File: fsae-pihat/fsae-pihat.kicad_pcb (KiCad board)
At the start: 4 copper layers, 85 x 56 mm, 67 parts, among them J1 Conn_02x02_Odd_Even, J2 Raspberry_Pi_4, J3 Conn_01x03_Pin, J4 1-2834011-4, J5 1-2834011-4, U1 TPS5430DDAR, U2 PCF8563T, U3 MCP2515-xST, U4 SN65HVD230DR-JSM, U5 TPS1H200AQDGNRQ1, X1 Q13FC1350000400, X2 X322512MSB4SI

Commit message: feat: readme, journal, pcb updates
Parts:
- added JP2: Jumper_3_Open, Connector_PinHeader_2.54mm:PinHeader_1x03_P2.54mm_Vertical, F.Cu at (187.3, 81.7)
- D11, D12, D2, D3: value SS34 -> SS54; footprint Diode_SMD:D_SMA -> PCM_JLCPCB:D_SMA
- moved D1 2.61 mm to (191.1, 83.8)
- moved D4 1.85 mm to (196.4, 92.2)
- moved J1 1.81 mm to (197.7, 86.0)
- moved F1 1.67 mm to (195.8, 81.8)
- moved J3 0.80 mm to (176.6, 103.5)
- moved D11 0.10 mm to (130.8, 116.8)
- moved D12 0.10 mm to (130.8, 113.0)
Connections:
- D1 pad 2: +24V-CAR -> /24V-RAW
- F1 pad 1: +24V-CAR -> /24V-RAW
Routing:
- net /CANL: track 23.8 -> 26.1 mm
- net /CANH: track 20.4 -> 22.4 mm
- net Net-(ETH1-A_YELLOW): track 20.5 -> 22.4 mm
- net GND: track 27.8 -> 27.1 mm
- net +24V-CAR: vias 52 -> 30
- added copper zone on F.Cu, net /24V-RAW
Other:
- board text added: "1.5A MAX"
- board text added: "EN"
- board text removed: "2A MAX"

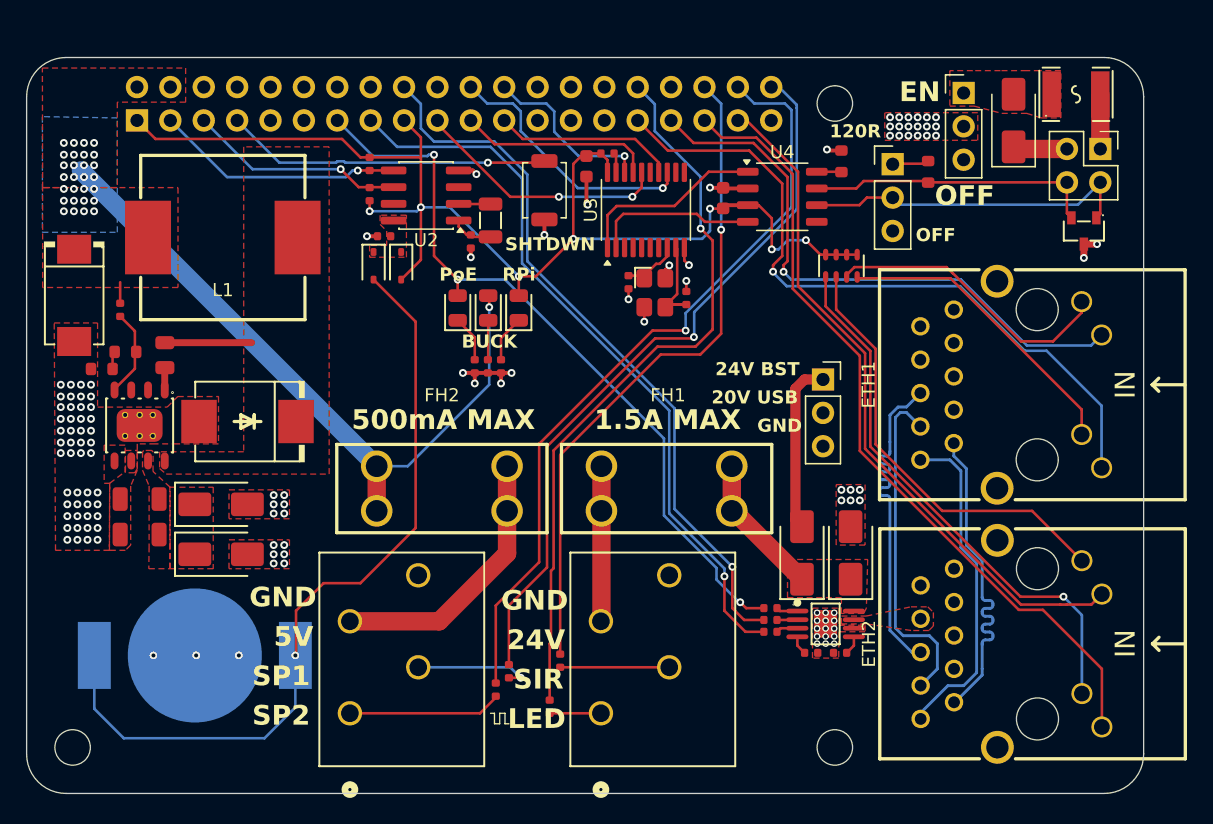
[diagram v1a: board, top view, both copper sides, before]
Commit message: feat: pcb art and updated design
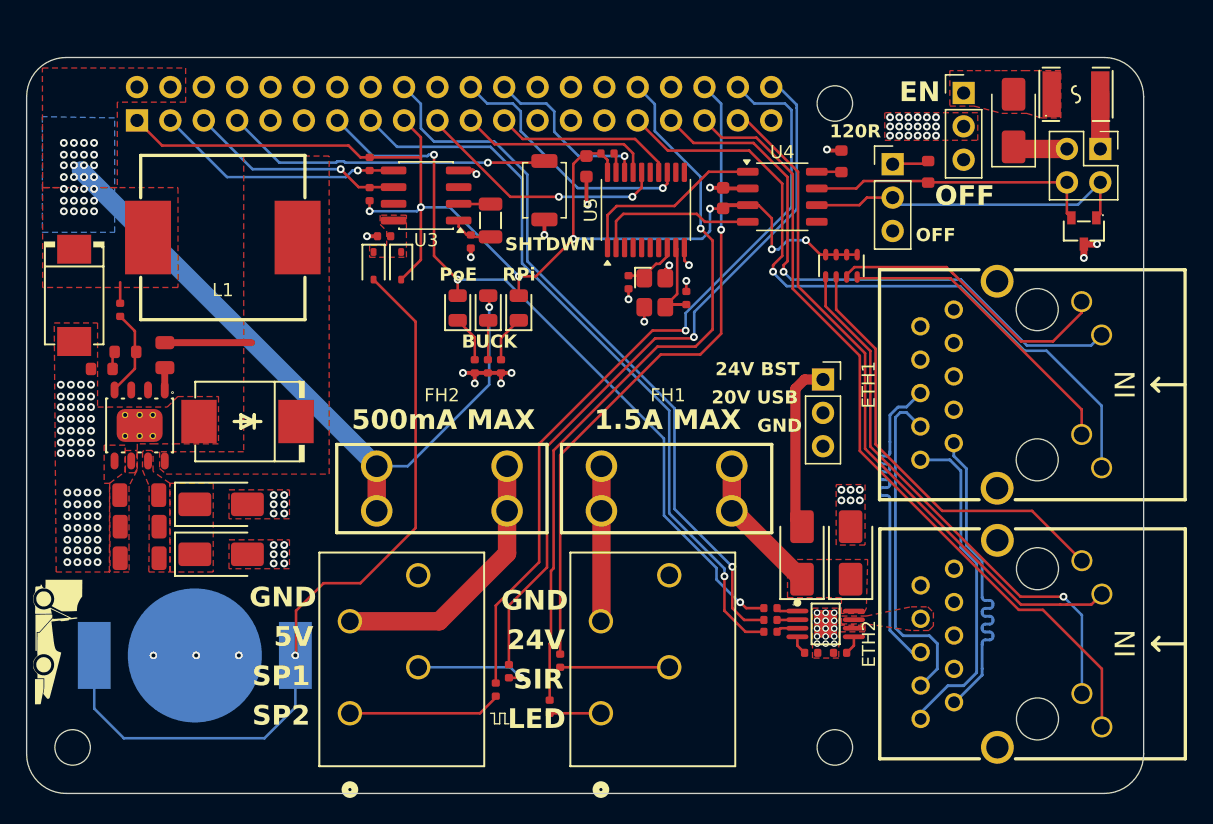
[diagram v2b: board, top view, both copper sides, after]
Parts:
- added C3: 4.7uF, PCM_JLCPCB:C_1206, F.Cu at (124.6, 117.1)
- added G***: LOGO, LOGO, F.Cu at (118.4, 123.5)
- added G***: LOGO, LOGO, B.Cu at (148.3, 96.8)
- added G***: LOGO, LOGO, B.Cu at (128.6, 90.7)
- moved C2 0.60 mm to (124.6, 114.7)
- moved C1 0.30 mm to (124.6, 112.3)
- renumbered C9 to C10, C8 to C11, C10 to C12, C3 to C4, C4 to C5, C5 to C7, C11 to C8, C7 to C9, D11 to D1, D8 to D10, D9 to D11, D10 to D12, D12 to D2, D5 to D3, D2 to D4, D3 to D5, D1 to D6, D6 to D7, D4 to D8, D7 to D9, J2 to J1, J4 to J2, J5 to J3, J3 to J4, J1 to J5, JP2 to JP1, JP1 to JP2, R6 to R1, R7 to R10, R8 to R11, R9 to R13, R10 to R14, R13 to R15, R14 to R16, R15 to R17, R16 to R18, R17 to R19, R1 to R2, R18 to R20, R2 to R3, R3 to R4, R4 to R5, R5 to R6, R19 to R7, R20 to R8, R11 to R9, U5 to U2, U2 to U3, U3 to U5
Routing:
- net GND: vias 84 -> 92
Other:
- board text added: "made by surya"

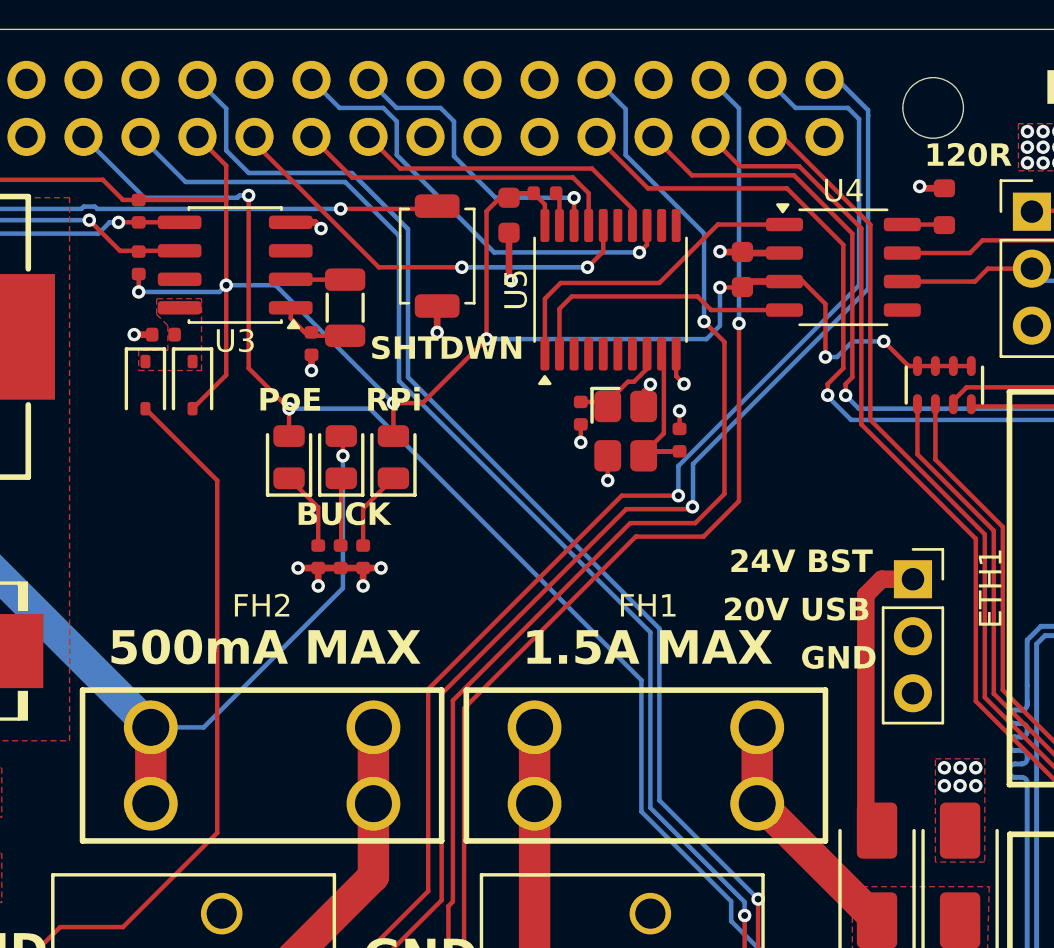
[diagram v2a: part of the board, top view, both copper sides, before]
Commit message: fix: missed hat pullup; feat: new pd module
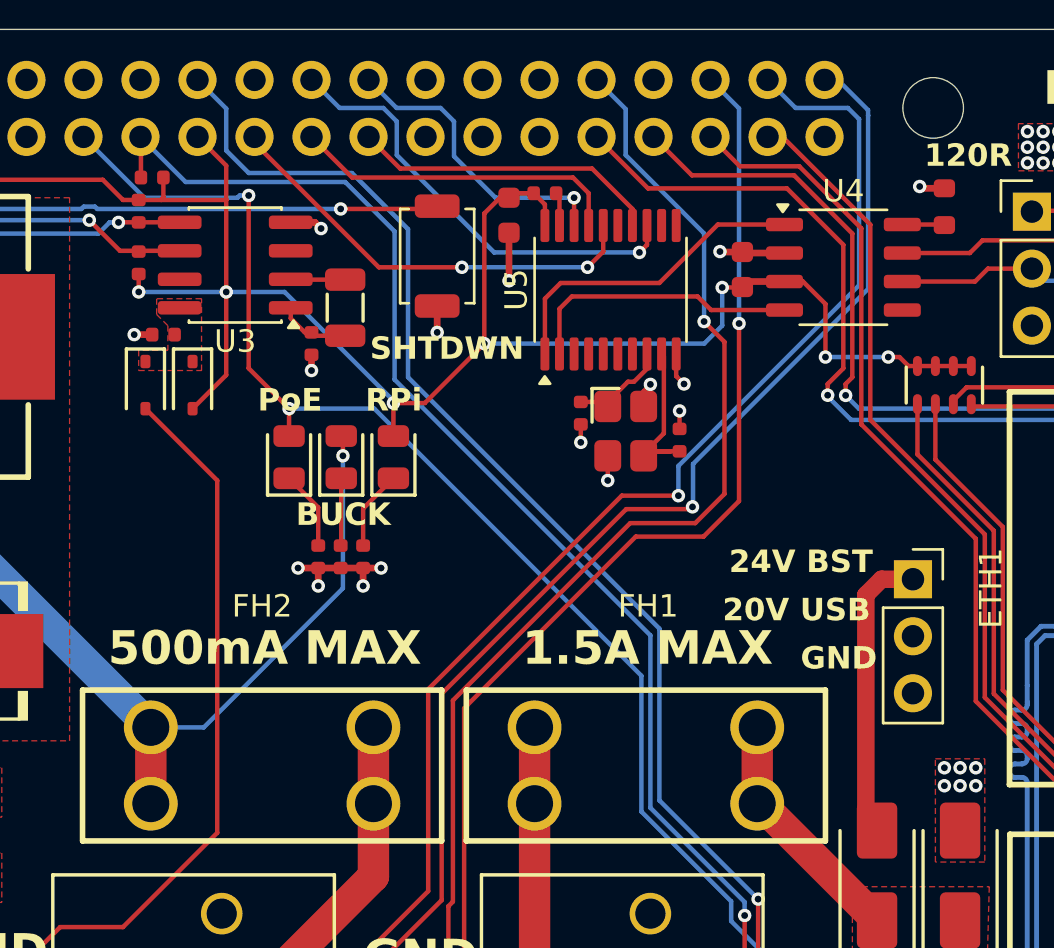
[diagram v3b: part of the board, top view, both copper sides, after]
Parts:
- added R21: 10kΩ, PCM_JLCPCB:R_0402, F.Cu at (142.7, 85.6)
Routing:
- net /PoE_READ: track 56.3 -> 58.1 mm
- net +3V3: track 94.2 -> 95.0 mm
